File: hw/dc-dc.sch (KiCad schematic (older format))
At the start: 0 parts

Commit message: hw: dc-dc page done
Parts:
- added C?: 0.47, symbol Device:C
- added C?: 0.01, symbol Device:C
- added C?: 1000.0 uF 10 V, symbol Device:CP
- added C?: 10.0 50V, symbol Device:C
- added DA?: LM2678SX-5.0/NOPB, symbol hat-ic:LM2678SX
- added L?: 12 uH SRR1208-120ML, symbol Device:L
- added VD?: PDS760-13, symbol Device:D_Schottky
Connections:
- new net: C?.2, DA?.3 (CB)
- new net +5V: C?.1, DA?.6 (FB), L?.2
- new net +BATT: C?.1, C?.1, DA?.2 (Input)
- new net GND: C?.2, C?.2, C?.2, DA?.4 (GND), VD?.2 (A)
- new net VSW: C?.1, DA?.1 (Switch_output), L?.1, VD?.1 (K)
- no-connect marks 0 -> 1
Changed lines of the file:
@@
 EELAYER 26 0
 EELAYER END
-$Descr A3 16535 11693
+$Descr A4 8268 11693 portrait
 encoding utf-8
 Sheet 7 7
 Title "OBC Drone Hat"
-Date "2018-03-21"
+Date "2018-04-08"
 Rev ""
 Comp "VEHQ"
@@
 Comment4 ""
 $EndDescr
-Text GLabel 3750 3700 0    60   UnSpc ~ 0
+Text GLabel 3150 4900 0    60   UnSpc ~ 0
 ADC_Vbat
-Text GLabel 3750 3800 0    60   UnSpc ~ 0
+Text GLabel 6500 5000 2    60   UnSpc ~ 0
 ADC_V5hat
+$Comp
+L power:+BATT #PWR?
+U 1 1 5AD5E52F
+P 2500 4950
+F 0 "#PWR?" H 2500 4800 50  0001 C CNN
+F 1 "+BATT" H 2515 5123 50  0000 C CNN
+F 2 "" H 2500 4950 50  0001 C CNN
+F 3 "" H 2500 4950 50  0001 C CNN
+	1    2500 4950
+	1    0    0    -1
+$EndComp
+$Comp
+L power:+5V #PWR?
+U 1 1 5AD5E558
+P 6350 4900
+F 0 "#PWR?" H 6350 4750 50  0001 C CNN
+F 1 "+5V" H 6365 5073 50  0000 C CNN
+F 2 "" H 6350 4900 50  0001 C CNN
+F 3 "" H 6350 4900 50  0001 C CNN
+	1    6350 4900
+	1    0    0    -1
+$EndComp
+$Comp
+L power:GND #PWR?
+U 1 1 5AD5E581
+P 4200 6550
+F 0 "#PWR?" H 4200 6300 50  0001 C CNN
+F 1 "GND" H 4205 6377 50  0000 C CNN
+F 2 "" H 4200 6550 50  0001 C CNN
+F 3 "" H 4200 6550 50  0001 C CNN
+	1    4200 6550
+	1    0    0    -1
+$EndComp
+$Comp
+L hat-ic:LM2678SX DA?
+U 1 1 5AD60FA4
+P 4200 5400
+F 0 "DA?" H 4200 6037 60  0000 C CNN
+F 1 "LM2678SX-5.0/NOPB" H 4200 5931 60  0000 C CNN
+F 2 "" H 4200 5400 60  0001 C CNN
+F 3 "" H 4200 5400 60  0001 C CNN
+	1    4200 5400
+	1    0    0    -1
+$EndComp
+$Comp
+L Device:L L?
+U 1 1 5AD61A2F
+P 5750 5500
+F 0 "L?" V 5850 5550 50  0000 C CNN
+F 1 "12 uH SRR1208-120ML" V 5650 5400 50  0000 C CNN
+F 2 "" H 5750 5500 50  0001 C CNN
+F 3 "~" H 5750 5500 50  0001 C CNN
+	1    5750 5500
+	0    -1   -1   0
+$EndComp
+$Comp
+L Device:D_Schottky VD?
+U 1 1 5AD61C7C
+P 5350 5950
+F 0 "VD?" V 5304 6029 50  0000 L CNN
+F 1 "PDS760-13" V 5395 6029 50  0000 L CNN
+F 2 "" H 5350 5950 50  0001 C CNN
+F 3 "~" H 5350 5950 50  0001 C CNN
+	1    5350 5950
+	0    1    1    0
+$EndComp
+$Comp
+L Device:C C?
+U 1 1 5AD61DB7
+P 2900 5550
+F 0 "C?" H 3015 5596 50  0000 L CNN
+F 1 "0.47" H 3015 5505 50  0000 L CNN
+F 2 "" H 2938 5400 50  0001 C CNN
+F 3 "~" H 2900 5550 50  0001 C CNN
+	1    2900 5550
+	1    0    0    -1
+$EndComp
+NoConn ~ 3550 5700
+Wire Wire Line
+	3550 5100 3250 5100
+Wire Wire Line
+	2500 5100 2500 4950
+Wire Wire Line
+	2900 5400 2900 5100
+Connection ~ 2900 5100
+Wire Wire Line
+	2900 5100 2500 5100
+Wire Wire Line
+	2500 5400 2500 5100
+Connection ~ 2500 5100
+Wire Wire Line
+	4200 6550 4200 6350
+Wire Wire Line
+	2500 5700 2500 6350
+Wire Wire Line
+	2500 6350 2900 6350
+Connection ~ 4200 6350
+Wire Wire Line
+	4200 6350 4200 6050
+Wire Wire Line
+	2900 5700 2900 6350
+Connection ~ 2900 6350
+Wire Wire Line
+	2900 6350 4200 6350
+Wire Wire Line
+	4850 5500 5350 5500
+Wire Wire Line
+	5350 5800 5350 5500
+Connection ~ 5350 5500
+Wire Wire Line
+	5350 5500 5600 5500
+Wire Wire Line
+	4200 6350 5350 6350
+Wire Wire Line
+	5350 6350 5350 6100
+$Comp
+L Device:C C?
+U 1 1 5AD6310A
+P 5100 5300
+F 0 "C?" V 5000 5200 50  0000 C CNN
+F 1 "0.01" V 5000 5450 50  0000 C CNN
+F 2 "" H 5138 5150 50  0001 C CNN
+F 3 "~" H 5100 5300 50  0001 C CNN
+	1    5100 5300
+	0    1    1    0
+$EndComp
+Wire Wire Line
+	4850 5300 4950 5300
+Wire Wire Line
+	5250 5300 5350 5300
+Wire Wire Line
+	5350 5300 5350 5500
+$Comp
+L Device:CP C?
+U 1 1 5AD6400F
+P 6350 5800
+F 0 "C?" H 6468 5846 50  0000 L CNN
+F 1 "1000.0 uF 10 V " H 6468 5755 50  0000 L CNN
+F 2 "" H 6388 5650 50  0001 C CNN
+F 3 "~" H 6350 5800 50  0001 C CNN
+	1    6350 5800
+	1    0    0    -1
+$EndComp
+Wire Wire Line
+	5900 5500 6100 5500
+Wire Wire Line
+	6350 5500 6350 5650
+Wire Wire Line
+	6350 4900 6350 5000
+Connection ~ 6350 5500
+Wire Wire Line
+	5350 6350 6350 6350
+Wire Wire Line
+	6350 6350 6350 5950
+Connection ~ 5350 6350
+Wire Wire Line
+	3150 4900 3250 4900
+Wire Wire Line
+	3250 4900 3250 5100
+Connection ~ 3250 5100
+Wire Wire Line
+	3250 5100 2900 5100
+Wire Wire Line
+	6350 5000 6500 5000
+Connection ~ 6350 5000
+Wire Wire Line
+	6350 5000 6350 5500
+Wire Wire Line
+	4850 5100 6100 5100
+Wire Wire Line
+	6100 5100 6100 5500
+Connection ~ 6100 5500
+Wire Wire Line
+	6100 5500 6350 5500
+Text Label 4850 5500 0    60   ~ 0
+VSW
+$Comp
+L Device:C C?
+U 1 1 5AD72B23
+P 2500 5550
+F 0 "C?" H 2350 5700 50  0000 L CNN
+F 1 "10.0 50V" H 2100 5400 50  0000 L CNN
+F 2 "" H 2538 5400 50  0001 C CNN
+F 3 "~" H 2500 5550 50  0001 C CNN
+	1    2500 5550
+	1    0    0    -1
+$EndComp
 $EndSCHEMATC

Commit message: hw: sch ready
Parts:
- gave numbers to parts that had none: 7
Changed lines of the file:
@@
 ADC_V5hat
 $Comp
-L power:+BATT #PWR?
+L power:+BATT #PWR060
 U 1 1 5AD5E52F
 P 2500 4950
-F 0 "#PWR?" H 2500 4800 50  0001 C CNN
+F 0 "#PWR060" H 2500 4800 50  0001 C CNN
 F 1 "+BATT" H 2515 5123 50  0000 C CNN
 F 2 "" H 2500 4950 50  0001 C CNN
@@
 $EndComp
 $Comp
-L power:+5V #PWR?
+L power:+5V #PWR059
 U 1 1 5AD5E558
 P 6350 4900
-F 0 "#PWR?" H 6350 4750 50  0001 C CNN
+F 0 "#PWR059" H 6350 4750 50  0001 C CNN
 F 1 "+5V" H 6365 5073 50  0000 C CNN
 F 2 "" H 6350 4900 50  0001 C CNN
@@
 $EndComp
 $Comp
-L power:GND #PWR?
+L power:GND #PWR061
 U 1 1 5AD5E581
 P 4200 6550
-F 0 "#PWR?" H 4200 6300 50  0001 C CNN
+F 0 "#PWR061" H 4200 6300 50  0001 C CNN
 F 1 "GND" H 4205 6377 50  0000 C CNN
 F 2 "" H 4200 6550 50  0001 C CNN
@@
 $EndComp
 $Comp
-L hat-ic:LM2678SX DA?
+L hat-ic:LM2678SX DA2
 U 1 1 5AD60FA4
 P 4200 5400
-F 0 "DA?" H 4200 6037 60  0000 C CNN
+F 0 "DA2" H 4200 6037 60  0000 C CNN
 F 1 "LM2678SX-5.0/NOPB" H 4200 5931 60  0000 C CNN
 F 2 "" H 4200 5400 60  0001 C CNN
@@
 $EndComp
 $Comp
-L Device:L L?
+L Device:L L1
 U 1 1 5AD61A2F
 P 5750 5500
-F 0 "L?" V 5850 5550 50  0000 C CNN
+F 0 "L1" V 5850 5550 50  0000 C CNN
 F 1 "12 uH SRR1208-120ML" V 5650 5400 50  0000 C CNN
 F 2 "" H 5750 5500 50  0001 C CNN
@@
 $EndComp
 $Comp
-L Device:D_Schottky VD?
+L Device:D_Schottky VD1
 U 1 1 5AD61C7C
 P 5350 5950
-F 0 "VD?" V 5304 6029 50  0000 L CNN
+F 0 "VD1" V 5304 6029 50  0000 L CNN
 F 1 "PDS760-13" V 5395 6029 50  0000 L CNN
 F 2 "" H 5350 5950 50  0001 C CNN
@@
 $EndComp
 $Comp
-L Device:C C?
+L Device:C C15
 U 1 1 5AD61DB7
 P 2900 5550
-F 0 "C?" H 3015 5596 50  0000 L CNN
+F 0 "C15" H 3015 5596 50  0000 L CNN
 F 1 "0.47" H 3015 5505 50  0000 L CNN
 F 2 "" H 2938 5400 50  0001 C CNN
@@
 	5350 6350 5350 6100
 $Comp
-L Device:C C?
+L Device:C C13
 U 1 1 5AD6310A
 P 5100 5300
-F 0 "C?" V 5000 5200 50  0000 C CNN
+F 0 "C13" V 5000 5200 50  0000 C CNN
 F 1 "0.01" V 5000 5450 50  0000 C CNN
 F 2 "" H 5138 5150 50  0001 C CNN
@@
 	5350 5300 5350 5500
 $Comp
-L Device:CP C?
+L Device:CP C16
 U 1 1 5AD6400F
 P 6350 5800
-F 0 "C?" H 6468 5846 50  0000 L CNN
+F 0 "C16" H 6468 5846 50  0000 L CNN
 F 1 "1000.0 uF 10 V " H 6468 5755 50  0000 L CNN
 F 2 "" H 6388 5650 50  0001 C CNN
@@
 VSW
 $Comp
-L Device:C C?
+L Device:C C14
 U 1 1 5AD72B23
 P 2500 5550
-F 0 "C?" H 2350 5700 50  0000 L CNN
+F 0 "C14" H 2350 5700 50  0000 L CNN
 F 1 "10.0 50V" H 2100 5400 50  0000 L CNN
 F 2 "" H 2538 5400 50  0001 C CNN

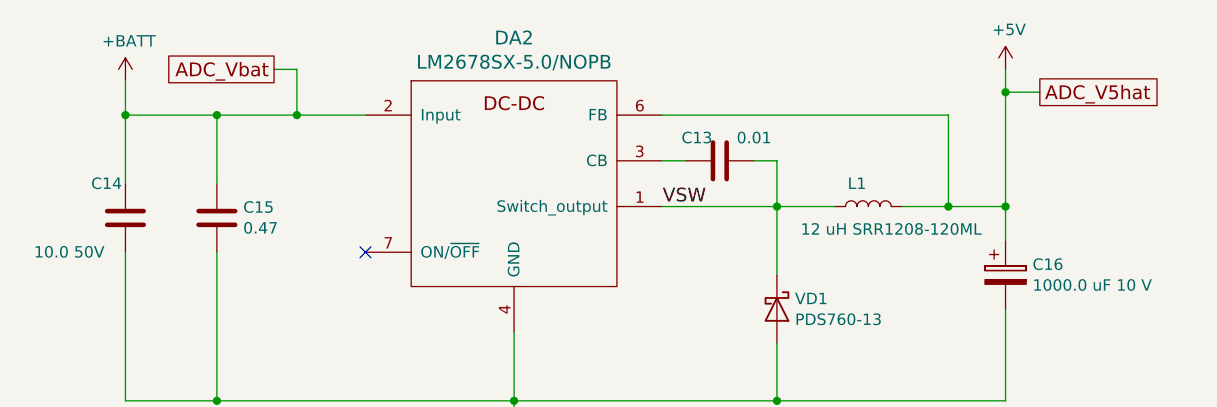
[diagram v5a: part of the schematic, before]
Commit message: hw: fix ERC
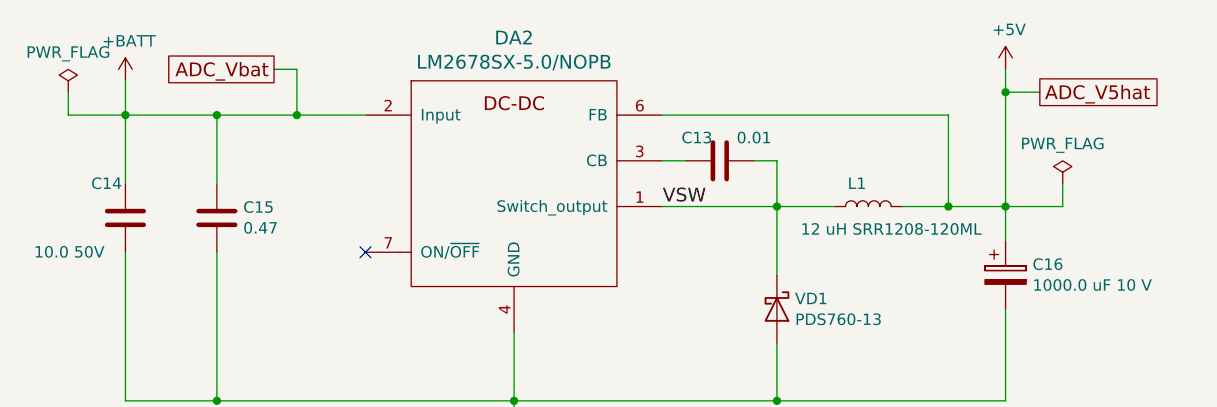
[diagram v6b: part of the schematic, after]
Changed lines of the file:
@@
 	1    0    0    -1
 $EndComp
+$Comp
+L power:PWR_FLAG #FLG0101
+U 1 1 5AE4DEDE
+P 6600 5400
+F 0 "#FLG0101" H 6600 5475 50  0001 C CNN
+F 1 "PWR_FLAG" H 6600 5574 50  0000 C CNN
+F 2 "" H 6600 5400 50  0001 C CNN
+F 3 "" H 6600 5400 50  0001 C CNN
+	1    6600 5400
+	1    0    0    -1
+$EndComp
+Wire Wire Line
+	6600 5400 6600 5500
+Wire Wire Line
+	6600 5500 6350 5500
+$Comp
+L power:PWR_FLAG #FLG0104
+U 1 1 5AE580C9
+P 2250 5000
+F 0 "#FLG0104" H 2250 5075 50  0001 C CNN
+F 1 "PWR_FLAG" H 2250 5174 50  0000 C CNN
+F 2 "" H 2250 5000 50  0001 C CNN
+F 3 "" H 2250 5000 50  0001 C CNN
+	1    2250 5000
+	1    0    0    -1
+$EndComp
+Wire Wire Line
+	2250 5000 2250 5100
+Wire Wire Line
+	2250 5100 2500 5100
 $EndSCHEMATC

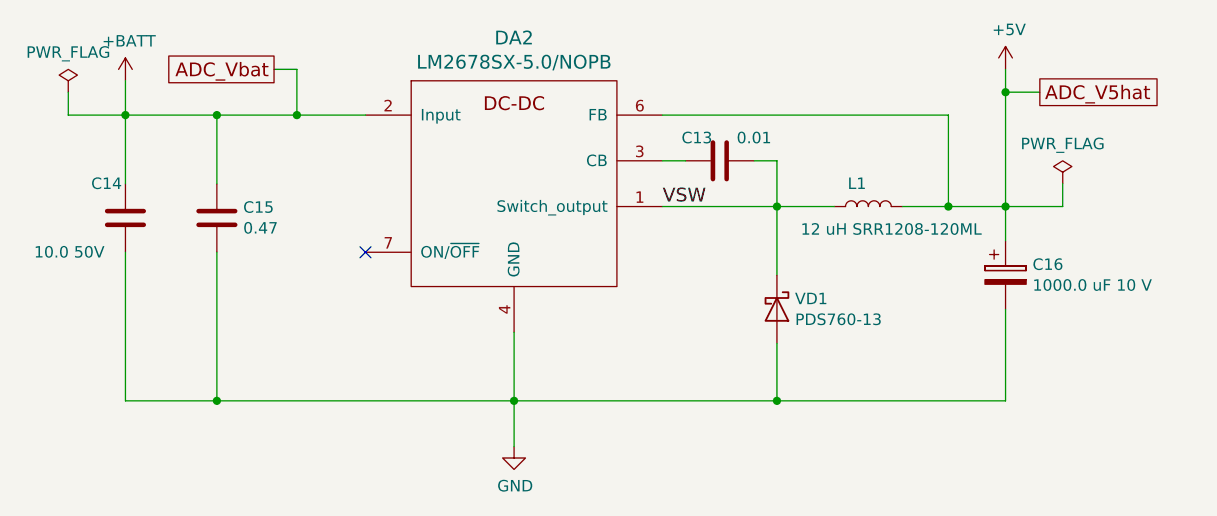
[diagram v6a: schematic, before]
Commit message: hw: cvpcb for R,C
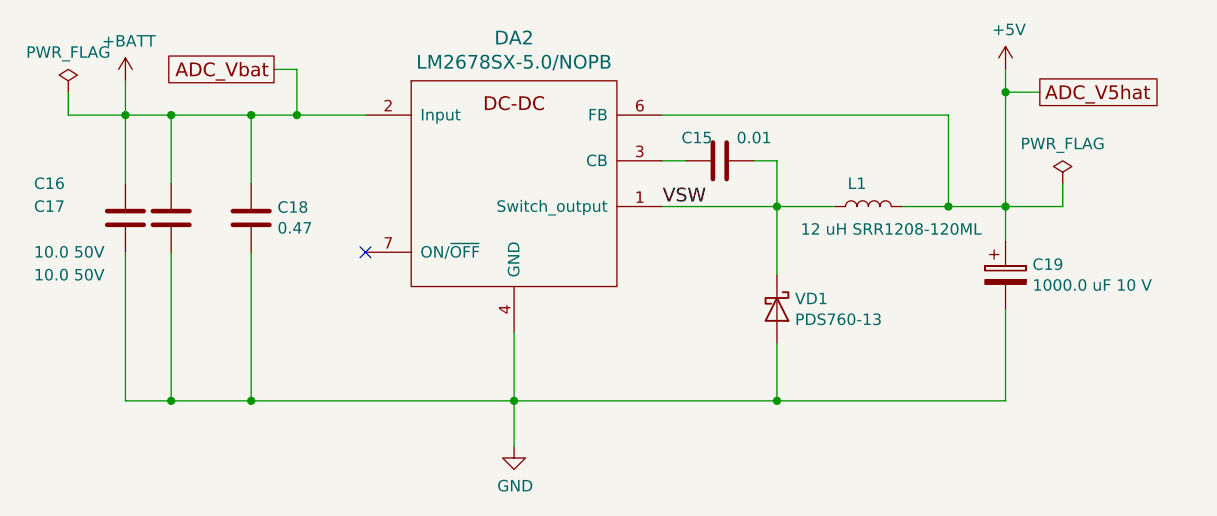
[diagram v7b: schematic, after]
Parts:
- added C17: 10.0 50V, Capacitor_SMD:C_1206_3216Metric_Pad1.24x1.80mm_HandSolder, symbol Device:C
- C15: renamed from C13; footprint (none) -> Capacitor_SMD:C_0603_1608Metric
- C16: renamed from C14; footprint (none) -> Capacitor_SMD:C_1206_3216Metric_Pad1.24x1.80mm_HandSolder
- C18: renamed from C15; footprint (none) -> Capacitor_SMD:C_1206_3216Metric_Pad1.24x1.80mm_HandSolder
- C19: renamed from C16; footprint (none) -> Capacitor_SMD:CP_Elec_10x10.5
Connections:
- net +BATT: now also C17.1
- net GND: now also C17.2
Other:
- moved on the sheet: C18
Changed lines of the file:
@@
 $EndComp
 $Comp
-L Device:C C15
+L Device:C C18
 U 1 1 5AD61DB7
-P 2900 5550
-F 0 "C15" H 3015 5596 50  0000 L CNN
-F 1 "0.47" H 3015 5505 50  0000 L CNN
-F 2 "" H 2938 5400 50  0001 C CNN
-F 3 "~" H 2900 5550 50  0001 C CNN
-	1    2900 5550
+P 3050 5550
+F 0 "C18" H 3165 5596 50  0000 L CNN
+F 1 "0.47" H 3165 5505 50  0000 L CNN
+F 2 "Capacitor_SMD:C_1206_3216Metric_Pad1.24x1.80mm_HandSolder" H 3088 5400 50  0001 C CNN
+F 3 "~" H 3050 5550 50  0001 C CNN
+	1    3050 5550
 	1    0    0    -1
 $EndComp
@@
 	2500 5100 2500 4950
 Wire Wire Line
-	2900 5400 2900 5100
-Connection ~ 2900 5100
+	3050 5400 3050 5100
+Connection ~ 3050 5100
 Wire Wire Line
-	2900 5100 2500 5100
+	3050 5100 2700 5100
 Wire Wire Line
 	2500 5400 2500 5100
@@
 	2500 5700 2500 6350
 Wire Wire Line
-	2500 6350 2900 6350
+	2500 6350 2700 6350
 Connection ~ 4200 6350
 Wire Wire Line
 	4200 6350 4200 6050
 Wire Wire Line
-	2900 5700 2900 6350
-Connection ~ 2900 6350
+	3050 5700 3050 6350
+Connection ~ 3050 6350
 Wire Wire Line
-	2900 6350 4200 6350
+	3050 6350 4200 6350
 Wire Wire Line
 	4850 5500 5350 5500
@@
 	5350 6350 5350 6100
 $Comp
-L Device:C C13
+L Device:C C15
 U 1 1 5AD6310A
 P 5100 5300
-F 0 "C13" V 5000 5200 50  0000 C CNN
+F 0 "C15" V 5000 5200 50  0000 C CNN
 F 1 "0.01" V 5000 5450 50  0000 C CNN
-F 2 "" H 5138 5150 50  0001 C CNN
+F 2 "Capacitor_SMD:C_0603_1608Metric" H 5138 5150 50  0001 C CNN
 F 3 "~" H 5100 5300 50  0001 C CNN
 	1    5100 5300
@@
 	5350 5300 5350 5500
 $Comp
-L Device:CP C16
+L Device:CP C19
 U 1 1 5AD6400F
 P 6350 5800
-F 0 "C16" H 6468 5846 50  0000 L CNN
+F 0 "C19" H 6468 5846 50  0000 L CNN
 F 1 "1000.0 uF 10 V " H 6468 5755 50  0000 L CNN
-F 2 "" H 6388 5650 50  0001 C CNN
+F 2 "Capacitor_SMD:CP_Elec_10x10.5" H 6388 5650 50  0001 C CNN
 F 3 "~" H 6350 5800 50  0001 C CNN
 	1    6350 5800
@@
 Connection ~ 3250 5100
 Wire Wire Line
-	3250 5100 2900 5100
+	3250 5100 3050 5100
 Wire Wire Line
 	6350 5000 6500 5000
@@
 VSW
 $Comp
-L Device:C C14
+L Device:C C16
 U 1 1 5AD72B23
 P 2500 5550
-F 0 "C14" H 2350 5700 50  0000 L CNN
+F 0 "C16" H 2100 5700 50  0000 L CNN
 F 1 "10.0 50V" H 2100 5400 50  0000 L CNN
-F 2 "" H 2538 5400 50  0001 C CNN
+F 2 "Capacitor_SMD:C_1206_3216Metric_Pad1.24x1.80mm_HandSolder" H 2538 5400 50  0001 C CNN
 F 3 "~" H 2500 5550 50  0001 C CNN
 	1    2500 5550
@@
 $EndComp
 $Comp
-L power:PWR_FLAG #FLG0101
+L power:PWR_FLAG #FLG05
 U 1 1 5AE4DEDE
 P 6600 5400
-F 0 "#FLG0101" H 6600 5475 50  0001 C CNN
+F 0 "#FLG05" H 6600 5475 50  0001 C CNN
 F 1 "PWR_FLAG" H 6600 5574 50  0000 C CNN
 F 2 "" H 6600 5400 50  0001 C CNN
@@
 	6600 5500 6350 5500
 $Comp
-L power:PWR_FLAG #FLG0104
+L power:PWR_FLAG #FLG04
 U 1 1 5AE580C9
 P 2250 5000
-F 0 "#FLG0104" H 2250 5075 50  0001 C CNN
+F 0 "#FLG04" H 2250 5075 50  0001 C CNN
 F 1 "PWR_FLAG" H 2250 5174 50  0000 C CNN
 F 2 "" H 2250 5000 50  0001 C CNN
@@
 Wire Wire Line
 	2250 5100 2500 5100
+$Comp
+L Device:C C17
+U 1 1 5AEABA88
+P 2700 5550
+F 0 "C17" H 2100 5600 50  0000 L CNN
+F 1 "10.0 50V" H 2100 5300 50  0000 L CNN
+F 2 "Capacitor_SMD:C_1206_3216Metric_Pad1.24x1.80mm_HandSolder" H 2738 5400 50  0001 C CNN
+F 3 "~" H 2700 5550 50  0001 C CNN
+	1    2700 5550
+	1    0    0    -1
+$EndComp
+Wire Wire Line
+	2700 5100 2700 5400
+Connection ~ 2700 5100
+Wire Wire Line
+	2700 5100 2500 5100
+Wire Wire Line
+	2700 5700 2700 6350
+Connection ~ 2700 6350
+Wire Wire Line
+	2700 6350 3050 6350
 $EndSCHEMATC

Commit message: hw: only custom packages left unassigned
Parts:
- DA2: footprint (none) -> Package_TO_SOT_SMD:TO-263-7_TabPin4
- L1: footprint (none) -> Inductor_SMD:L_12x12mm_H8mm
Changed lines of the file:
@@
 F 0 "DA2" H 4200 6037 60  0000 C CNN
 F 1 "LM2678SX-5.0/NOPB" H 4200 5931 60  0000 C CNN
-F 2 "" H 4200 5400 60  0001 C CNN
+F 2 "Package_TO_SOT_SMD:TO-263-7_TabPin4" H 4200 5400 60  0001 C CNN
 F 3 "" H 4200 5400 60  0001 C CNN
 	1    4200 5400
@@
 F 0 "L1" V 5850 5550 50  0000 C CNN
 F 1 "12 uH SRR1208-120ML" V 5650 5400 50  0000 C CNN
-F 2 "" H 5750 5500 50  0001 C CNN
+F 2 "Inductor_SMD:L_12x12mm_H8mm" H 5750 5500 50  0001 C CNN
 F 3 "~" H 5750 5500 50  0001 C CNN
 	1    5750 5500
